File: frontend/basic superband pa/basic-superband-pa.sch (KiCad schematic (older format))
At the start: 68 parts, among them CN1 EDGE, K1 D3002, K2 D3002, P1 BNC, P2 CONN_02X01, Q1 NPN, Q2 PNP, Q2-next FDV301, Q3 RD16HHF1, T1 TRANSFO, T2 8:1, T3 4:1, T4 OUT_TRANSF, U1 LP2951-50D

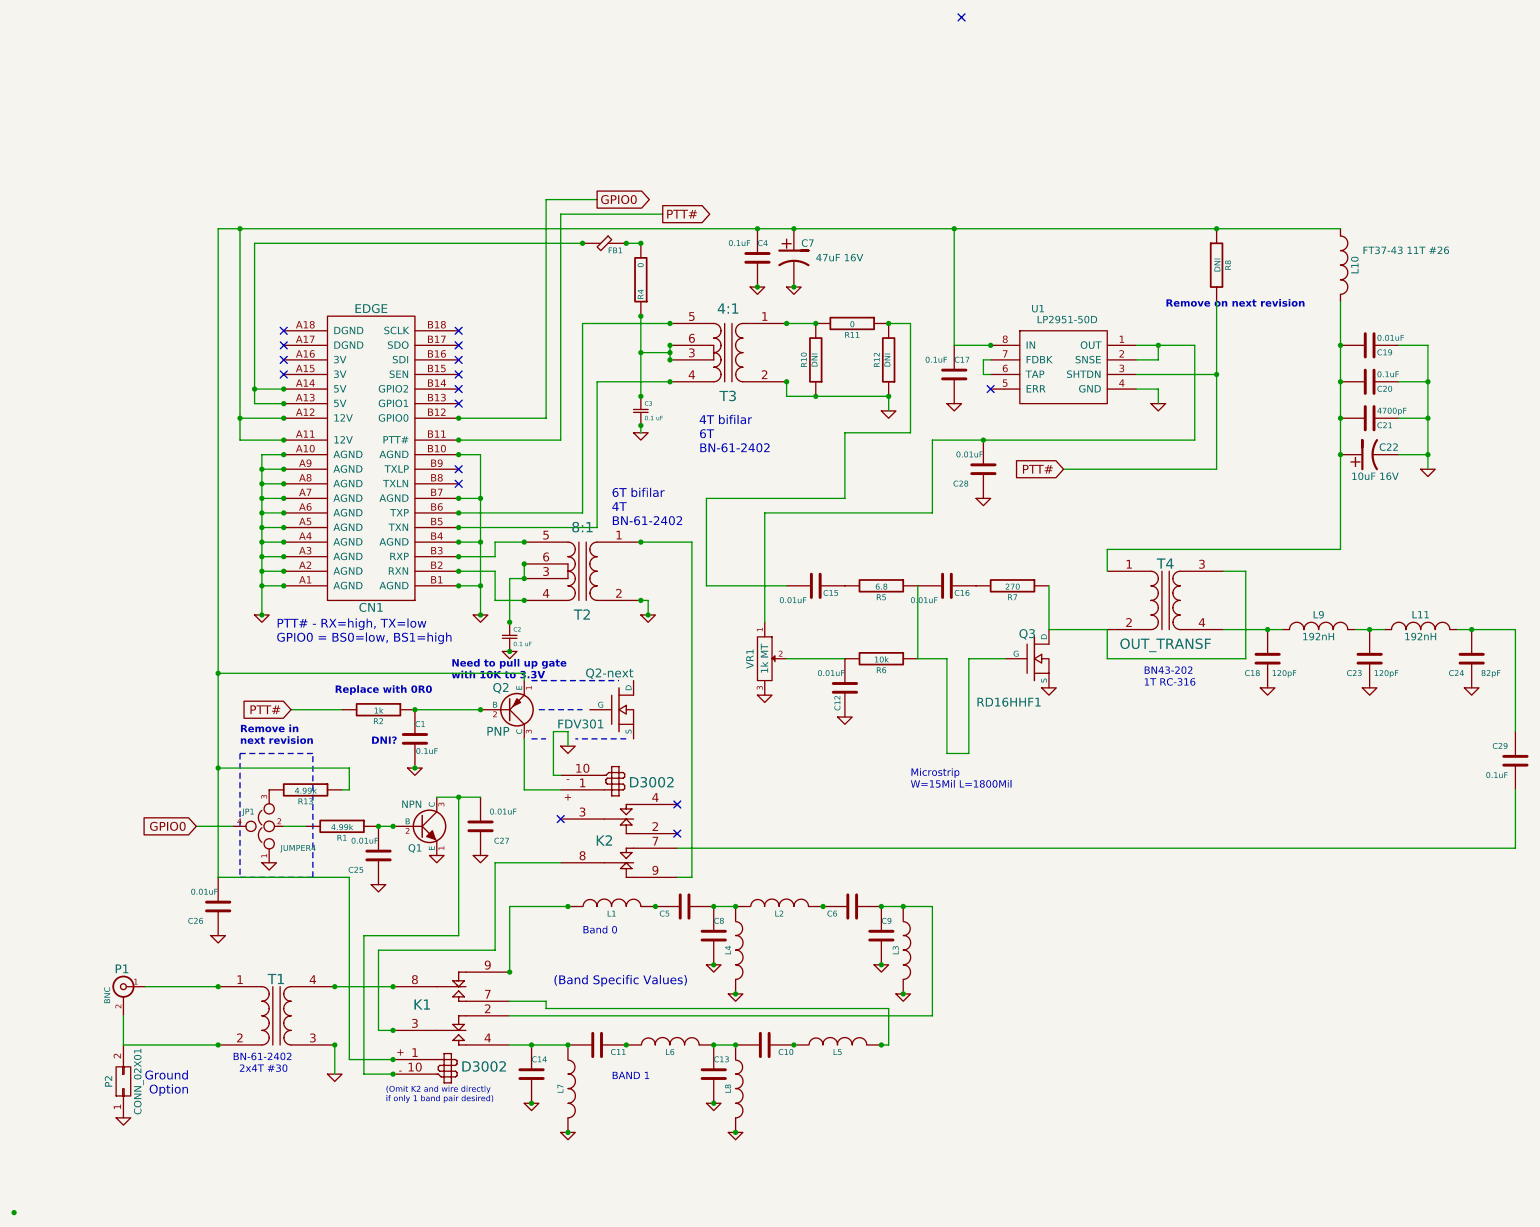
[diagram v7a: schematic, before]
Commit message: PTT change
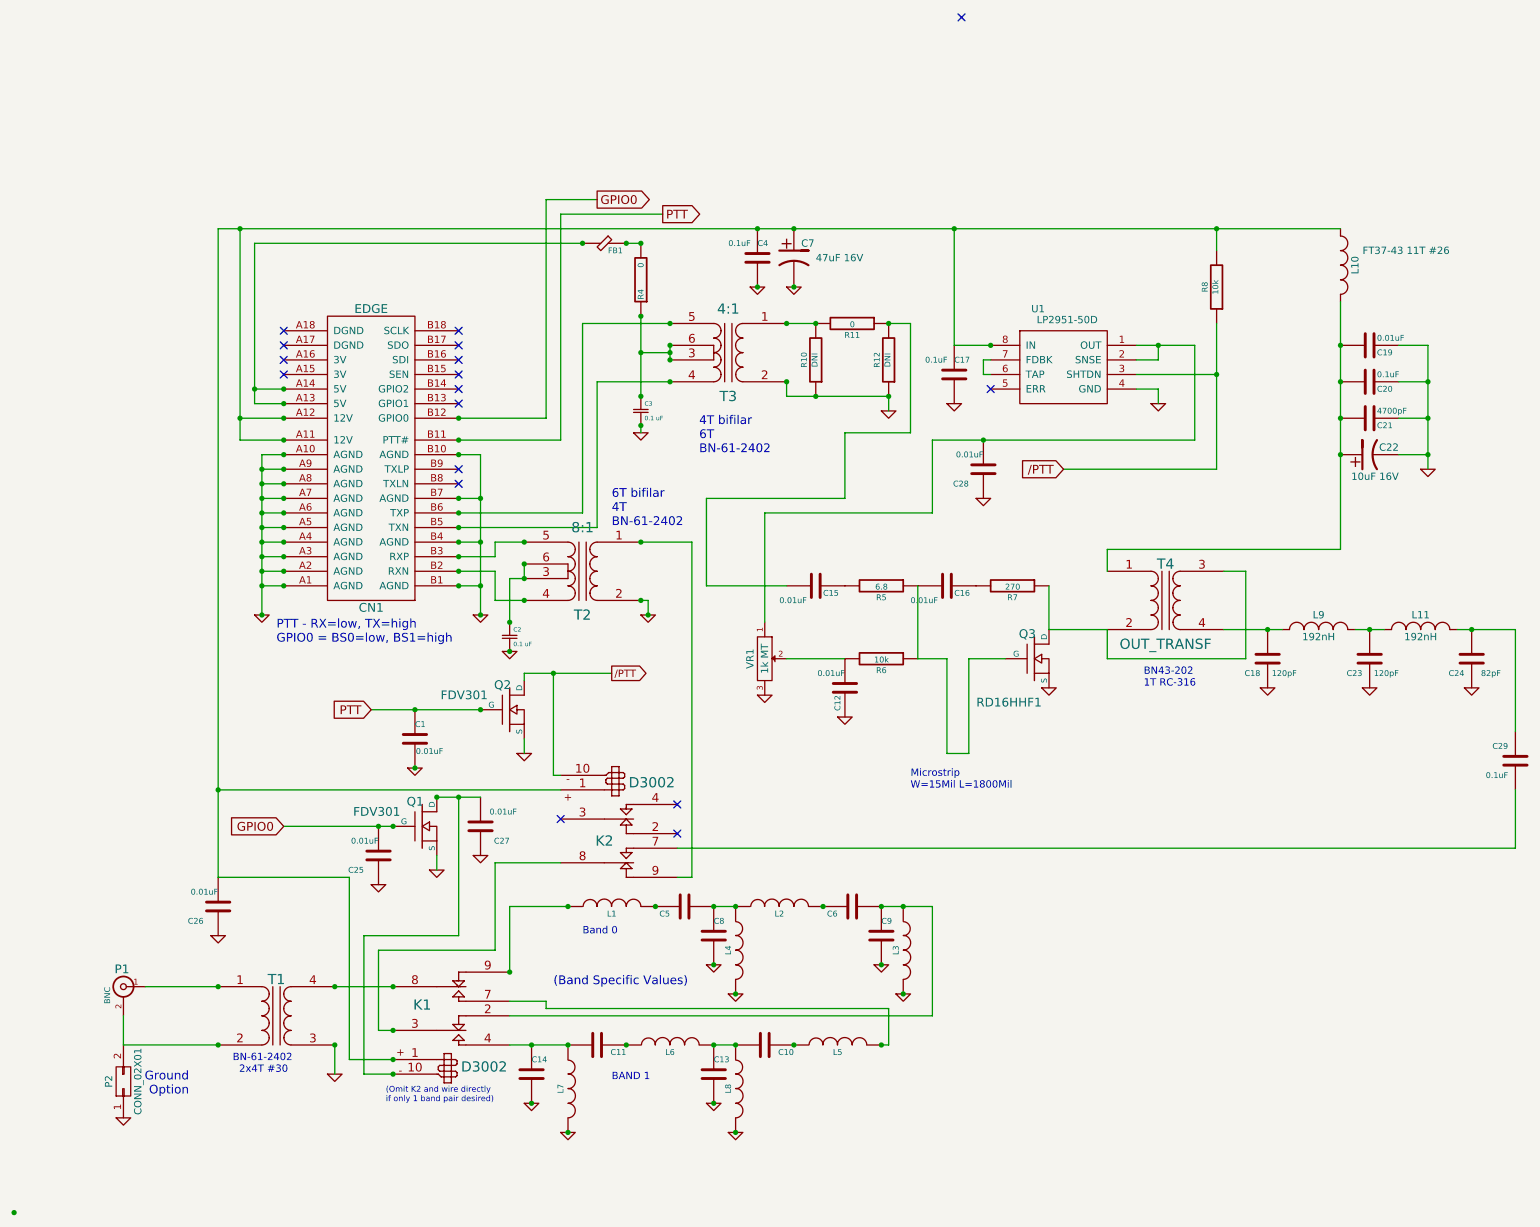
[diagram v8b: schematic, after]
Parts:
- removed JP1: JUMPER4, HERMESLITE:JUMPER4, symbol JUMPER4
- removed Q1: NPN, Transistors_SMD:sot23, symbol NPN
- removed Q2: PNP, Transistors_SMD:sot23, symbol PNP
- removed Q2-next: FDV301, symbol MOS_N
- removed R1, R13: 4.99k, HERMESLITE:R_0805, symbol R
- removed R2: 1k, HERMESLITE:R_0805, symbol R
- added Q1, Q2: FDV301, SMD_Packages:SOT-23-GDS, symbol MOS_N
- C1: value 0.1uF -> 0.01uF
- FB1: footprint SMD_Packages:SMD-1206 -> SMD_Packages:SMD-0805
- R10, R11, R12, R4, R5, R6, R7: footprint HERMESLITE:R_0805 -> Resistors_SMD:R_0805_HandSoldering
- R8: value DNI -> 10k; footprint HERMESLITE:R_0805 -> Resistors_SMD:R_0805_HandSoldering
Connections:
- net GND: now also Q1.S, Q2.S; no longer K2.10 (-)
- net GPIO0: now also C25.2, Q1.G
- net at C17.1, C26.2, C4.1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: now also K2.1 (+), R8.2; no longer R8.1
- net PTT: now reaches C1.1
- net PTT: now also CN1.B11 (PTT#), Q2.G
- net at C27.2, K1.10 (-): now also Q1.D
- removed net PTT#: CN1.B11 (PTT#), R8.2, U1.3 (SHTDN)
- new net /PTT: K2.10 (-), Q2.D, R8.1, U1.3 (SHTDN)
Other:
- note added: "PTT - RX=low, TX=high\nGPIO0 = BS0=low, BS1=high"
- note removed: "DNI?"
- note removed: "Need to pull up gate\nwith 10K to 3.3V"
- note removed: "PTT# - RX=high, TX=low\nGPIO0 = BS0=low, BS1=high"
- note removed: "Remove in\nnext revision"
- note removed: "Remove on next revision"
- note removed: "Replace with 0R0"
